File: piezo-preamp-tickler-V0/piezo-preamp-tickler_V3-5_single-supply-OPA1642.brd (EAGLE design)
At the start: 100.3 x 20.1 mm, 58 parts, among them IC1 OPA1642, IC2 DMN2400, IC3 BQ21040, IC4 BQ297X, IC5 SC4503, IC6 TPS7A49, J1 HEADPHONES, J2 PHONE, J3 Mixer, J5 Battery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

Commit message: boards layed out
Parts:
- C10: value 2.2pf -> 2.2pF; device adafruit:C0603 -> rcl:C0603
- C11: device adafruit:C0603 -> rcl:C1206
- C12, C13, C14, C15, C8: device adafruit:C0603 -> rcl:C0603
- C6, C7: device adafruit:C0805K -> rcl:C0603
- C9: value 56nf -> 56nF; device adafruit:C0603 -> rcl:C0603
- moved C8 60.5 mm to (3.83, 2.81), turned to 0 degrees
- moved C12 48.2 mm to (64.3, 9.63), turned to 180 degrees
- moved C13 47.1 mm to (64.4, 6.02), turned to 180 degrees
- moved C15 42.4 mm to (68.0, 18.0), turned to 180 degrees
- moved C9 42.4 mm to (27.8, 6.52), turned to 0 degrees
- moved C14 41.8 mm to (64.6, 18.0), turned to 0 degrees
- moved R18 26.0 mm to (21.4, 18.3)
- moved C10 21.0 mm to (26.4, 14.2)
- moved C11 17.6 mm to (47.0, 15.0), turned to 0 degrees
- moved C6 7.94 mm to (71.4, 18.0)
- moved R16 4.08 mm to (68.0, 9.66), turned to 180 degrees
- moved R21 2.30 mm to (21.5, 8.42)
- moved R13 2.00 mm to (52.0, 6.66)
- moved R3 2.00 mm to (31.2, 6.51)
- moved C7 1.10 mm to (68.0, 6.00)
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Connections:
- net GND2: now also C7.1; no longer C7.2
- net N$42: now also C7.2; no longer C7.1
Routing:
- net +12V: track 13.4 -> 76.5 mm, vias 0 -> 3
- net V+: track 112.2 -> 163.8 mm, vias 5 -> 3
- net N$30: track 19.5 -> 68.3 mm, vias 2 -> 4
- net VBAT: track 77.0 -> 124.9 mm, vias 3 -> 4
- net N$28: track 10.3 -> 55.7 mm, vias 0 -> 6
- net N$26: track 12.0 -> 55.1 mm, vias 0 -> 3
- net GND2: track 95.1 -> 70.9 mm, vias 4 -> 5
- net N$29: track 30.3 -> 51.7 mm, vias 0 -> 2
- net N$25: track 48.0 -> 65.0 mm, vias 3 -> 4
- net N$45: track 22.0 -> 7.25 mm, vias 0 -> 2
- net N$7: track 32.1 -> 42.9 mm, vias 0 -> 1
- net N$11: track 25.2 -> 35.6 mm, vias 1 -> 3
- net N$16: track 22.3 -> 31.0 mm
- net GND: track 220.8 -> 215.1 mm, vias 3 -> 2
- net N$2: track 29.4 -> 24.4 mm, vias 1 -> 0
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
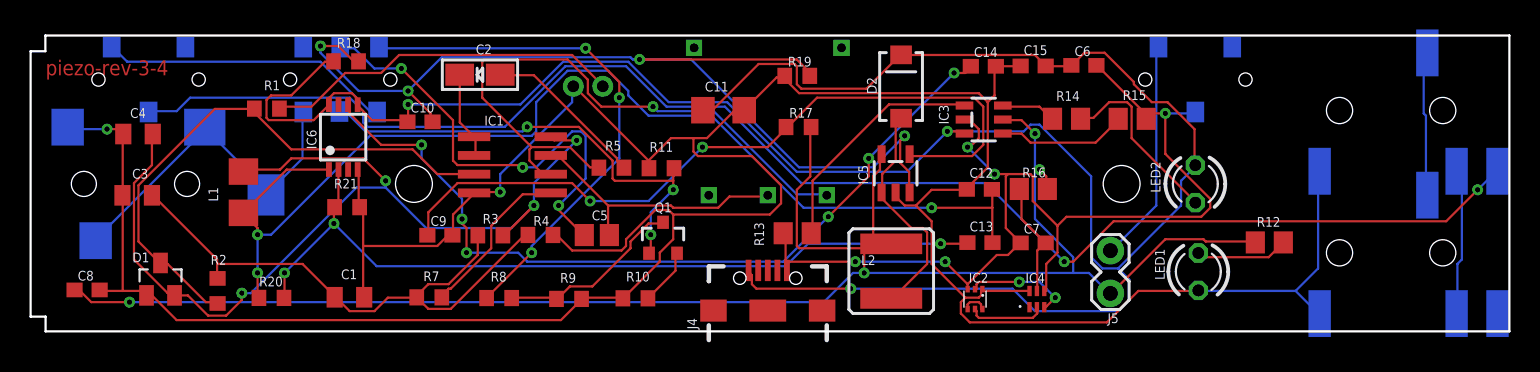
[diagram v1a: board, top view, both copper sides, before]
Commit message: piezo and mems preamps updates
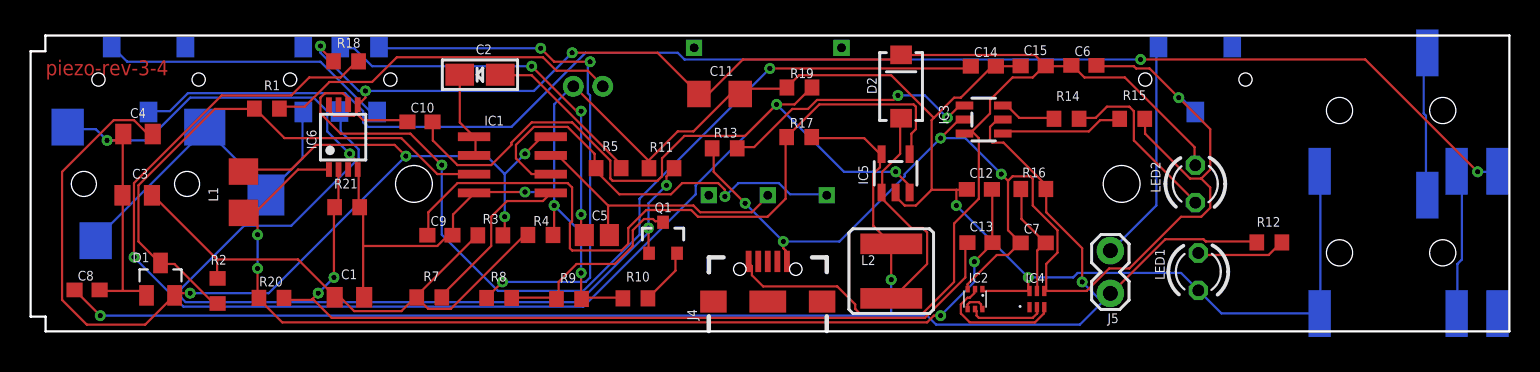
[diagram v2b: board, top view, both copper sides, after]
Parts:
- R12, R13, R14, R15, R16: device CMU-ArtFab:R0805 -> CMU-ArtFab:R0603
- moved R13 7.58 mm to (47.1, 12.4)
- moved C11 1.13 mm to (46.7, 16.1)
- moved R19 0.80 mm to (52.1, 16.5)
- moved R17 0.68 mm to (52.1, 13.2)
- moved J4 0.61 mm to (50.0, 2.02)
- moved R5 0.19 mm to (39.2, 11.1)
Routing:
- net N$30: track 68.3 -> 121.1 mm, vias 4 -> 3
- net V+: track 163.8 -> 113.9 mm
- net GND: track 215.1 -> 177.0 mm, vias 2 -> 7
- net SELECT: track 32.1 -> 60.6 mm, vias 3 -> 2
- net GND2: track 70.9 -> 88.0 mm
- net N$7: track 42.9 -> 29.6 mm
- net N$25: track 65.0 -> 73.2 mm
- net N$28: track 55.7 -> 63.3 mm, vias 6 -> 2
- net VBAT: track 124.9 -> 117.9 mm, vias 4 -> 3
- net +12V: track 76.5 -> 71.2 mm, vias 3 -> 4
- net N$26: track 55.1 -> 60.0 mm, vias 3 -> 2
- net N$16: track 31.0 -> 26.7 mm
- net N$17: track 102.9 -> 98.8 mm
- net N$36: track 16.1 -> 17.9 mm, vias 0 -> 2
- net N$45: track 7.25 -> 8.69 mm, vias 2 -> 0
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
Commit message: upates
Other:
- board text added: "piezo-rev-3-5"
- board text removed: "piezo-rev-3-4"
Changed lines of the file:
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@@
 <?xml version="1.0" encoding="utf-8"?>
 <!DOCTYPE eagle SYSTEM "eagle.dtd">
-<eagle version="8.2.2">
+<eagle version="8.3.1">
 <drawing>
 <settings>
 <setting alwaysvectorfont="no"/>
+<setting keepoldvectorfont="yes"/>
 <setting verticaltext="up"/>
 </settings>
@@
 <wire x1="0" y1="19" x2="0" y2="1" width="0.1524" layer="20"/>
 <wire x1="1.016" y1="0" x2="100.3" y2="0" width="0.1524" layer="20"/>
-<text x="1.016" y="17.367" size="1.016" layer="1">piezo-rev-3-4</text>
+<text x="1.716" y="17.687" size="0.6096" layer="1" font="vector">piezo-rev-3-5</text>
 <wire x1="0" y1="1" x2="1.016" y2="1" width="0.1524" layer="20"/>
 <wire x1="1.016" y1="1" x2="1.016" y2="0" width="0.1524" layer="20"/>
@@
 <compatibility>
 <note version="8.2" severity="warning">
-Since Version 8.2, Eagle supports online libraries. The ids
+Since Version 8.2, EAGLE supports online libraries. The ids
 of those online libraries will not be understood (or retained)
 with this version.
